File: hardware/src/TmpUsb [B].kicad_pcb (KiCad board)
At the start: 2 copper layers, 25 x 17 mm, 16 parts, among them P1 48037-2200, U1 PIC18F26J50

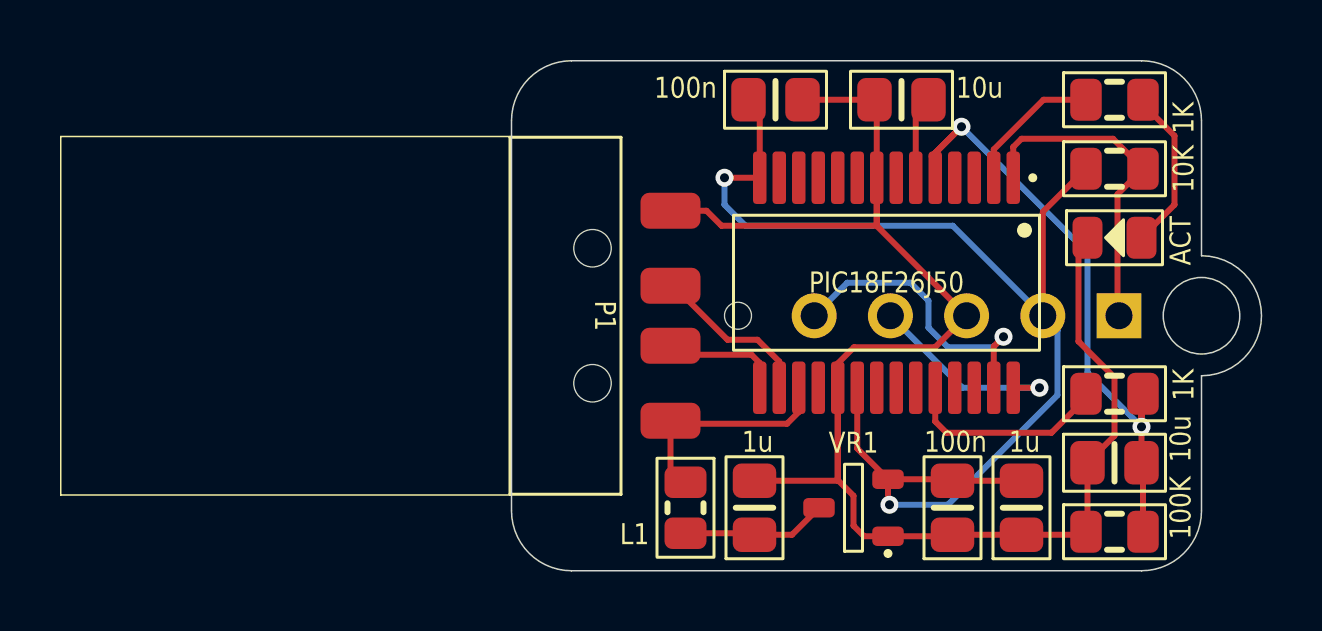
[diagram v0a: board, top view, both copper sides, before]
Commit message: Fixed USB connector DRC checks
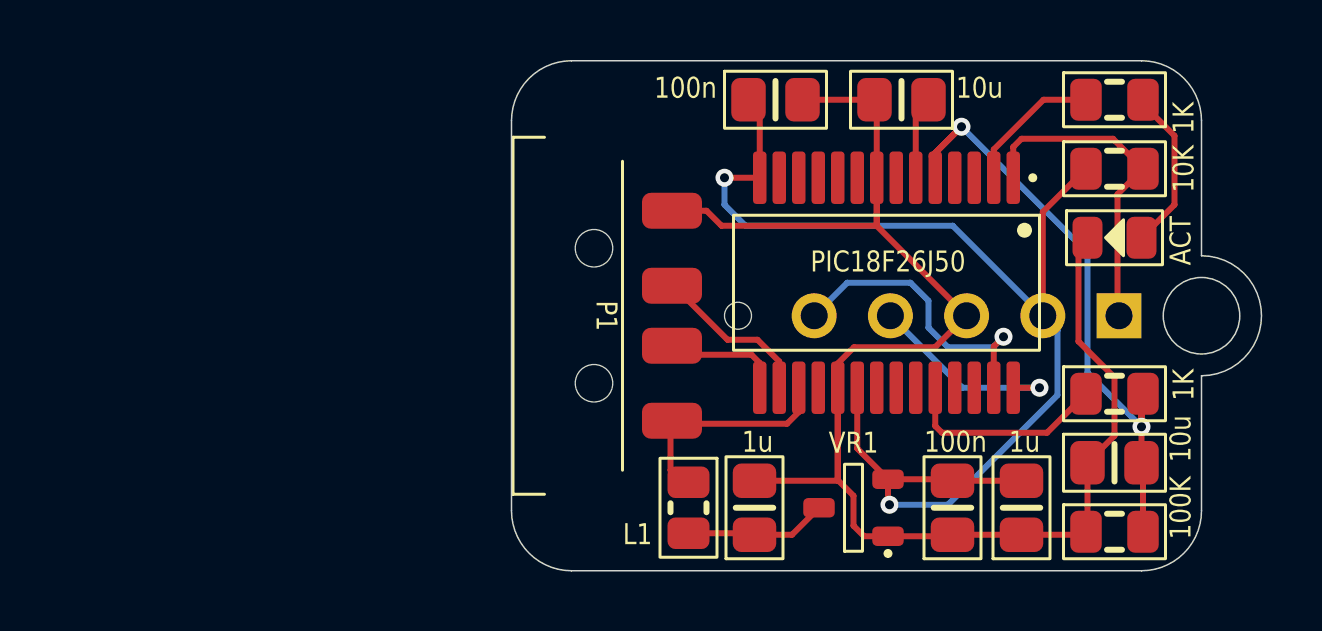
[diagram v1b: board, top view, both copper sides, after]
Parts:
- moved L1 0.10 mm to (25.9, 34.9)
- moved P1 0.05 mm to (22.8, 28.5)
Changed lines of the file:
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@@
   )
   (footprint "Medo64-SMD:L (0805)" (layer "F.Cu")
-    (at 25.8 34.9 -90)
+    (at 25.9 34.9 -90)
     (descr "RESC2013X70N")
     (attr smd)
@@
   )
   (footprint "Medo64-SMD:P USB 2.0 (4w)" (layer "F.Cu")
-    (at 22.7 28.5 -90)
+    (at 22.75 28.5 -90)
     (attr smd)
     (fp_text reference "P1" (at 0 0 -90 unlocked) (layer "F.SilkS")
@@
     (fp_text value "48037-2200" (at 0 0.825 -90 unlocked) (layer "F.SilkS") hide
         (effects (font (size 0.7 0.6) (thickness 0.1)) (justify top))
+    )
+    (fp_text user "D-" (at 1 -1.5 -90 unlocked) (layer "User.7")
+        (effects (font (size 0.13 0.07) (thickness 0.01)) (justify top))
+    )
+    (fp_text user "Vbus" (at 3.5 -1.5 -90 unlocked) (layer "User.7")
+        (effects (font (size 0.13 0.07) (thickness 0.014) bold) (justify top))
+    )
+    (fp_text user "D+" (at -1 -1.5 -90 unlocked) (layer "User.7")
+        (effects (font (size 0.13 0.07) (thickness 0.01)) (justify top))
     )
     (fp_text user "GND" (at -3.5 -1.5 -90 unlocked) (layer "User.7")
         (effects (font (size 0.13 0.07) (thickness 0.014) bold) (justify top))
     )
-    (fp_text user "D+" (at -1 -1.5 -90 unlocked) (layer "User.7")
-        (effects (font (size 0.13 0.07) (thickness 0.01)) (justify top))
-    )
-    (fp_text user "Vbus" (at 3.5 -1.5 -90 unlocked) (layer "User.7")
-        (effects (font (size 0.13 0.07) (thickness 0.014) bold) (justify top))
-    )
-    (fp_text user "D-" (at 1 -1.5 -90 unlocked) (layer "User.7")
-        (effects (font (size 0.13 0.07) (thickness 0.01)) (justify top))
-    )
-    (fp_line (start -5.975 2.75) (end -5.975 17.725)
-      (stroke (width 0.05) (type default)) (layer "F.SilkS"))
-    (fp_line (start -5.975 17.725) (end 5.975 17.725)
-      (stroke (width 0.05) (type default)) (layer "F.SilkS"))
-    (fp_line (start -5.95 -0.95) (end -5.95 2.75)
+    (fp_line (start -5.95 1.65) (end -5.95 2.7)
       (stroke (width 0.1) (type default)) (layer "F.SilkS"))
-    (fp_line (start -5.95 -0.95) (end 5.95 -0.95)
+    (fp_line (start -5.95 2.7) (end 5.95 2.7)
       (stroke (width 0.1) (type default)) (layer "F.SilkS"))
-    (fp_line (start -5.95 2.75) (end 5.95 2.75)
+    (fp_line (start -5.15 -0.95) (end 5.15 -0.95)
       (stroke (width 0.1) (type default)) (layer "F.SilkS"))
-    (fp_line (start 5.95 -0.95) (end 5.95 2.75)
+    (fp_line (start 5.95 1.65) (end 5.95 2.7)
       (stroke (width 0.1) (type default)) (layer "F.SilkS"))
-    (fp_line (start 5.975 2.75) (end 5.975 17.725)
-      (stroke (width 0.05) (type default)) (layer "F.SilkS"))
-    (fp_rect (start -7 -4.1) (end 7 18.25)
-      (stroke (width 0.01) (type dash)) (fill none) (layer "F.CrtYd"))
+    (fp_line (start -7 -2.1) (end -4.6 -2.1)
+      (stroke (width 0.01) (type dash)) (layer "F.CrtYd"))
+    (fp_line (start -7 18.25) (end -7 -2.1)
+      (stroke (width 0.01) (type dash)) (layer "F.CrtYd"))
+    (fp_line (start -7 18.25) (end 7 18.25)
+      (stroke (width 0.01) (type dash)) (layer "F.CrtYd"))
+    (fp_line (start -4.6 -4.1) (end 4.6 -4.1)
+      (stroke (width 0.01) (type dash)) (layer "F.CrtYd"))
+    (fp_line (start -4.6 -2.1) (end -4.6 -4.1)
+      (stroke (width 0.01) (type dash)) (layer "F.CrtYd"))
+    (fp_line (start 4.6 -2.1) (end 4.6 -4.1)
+      (stroke (width 0.01) (type dash)) (layer "F.CrtYd"))
+    (fp_line (start 4.6 -2.1) (end 7 -2.1)
+      (stroke (width 0.01) (type dash)) (layer "F.CrtYd"))
+    (fp_line (start 7 18.25) (end 7 -2.1)
+      (stroke (width 0.01) (type dash)) (layer "F.CrtYd"))
+    (fp_line (start -6 2.75) (end 6 2.75)
+      (stroke (width 0.01) (type dash_dot)) (layer "F.Fab"))
     (fp_rect (start -6 17.75) (end 6 -1)
       (stroke (width 0.01) (type dash_dot)) (fill none) (layer "F.Fab"))
@@
     (pad "4" smd roundrect (at -3.5 -2.6 270) (size 1.2 2) (layers "F.Cu" "F.Paste" "F.Mask") (roundrect_rratio 0.25)
       (net 5 "GND") (thermal_bridge_angle 45))
-    (model "Models/480372200.stp"
+    (model "../../3dmodels/Medo64-SMD.3dshapes/480372200.step"
       (offset (xyz 0 -8.375 0))
       (scale (xyz 1 1 1))
@@
         (effects (font (size 0.7 0.6) (thickness 0.1)) (justify bottom))
     )
-    (fp_text value "PIC18F26J50" (at 0 0 unlocked) (layer "F.SilkS")
+    (fp_text value "PIC18F26J50" (at -0.7 -0.05 unlocked) (layer "F.SilkS")
         (effects (font (size 0.7 0.6) (thickness 0.1)))
     )
@@
   (segment (start 39.2 26.4) (end 39.2 30.4) (width 0.2) (layer "B.Cu") (net 7))
   (segment (start 35 22.2) (end 39.2 26.4) (width 0.2) (layer "B.Cu") (net 7))
-  (segment (start 39.15 31.25) (end 38 32.4) (width 0.2) (layer "F.Cu") (net 8))
-  (segment (start 34.5 32.4) (end 34.125 32.025) (width 0.2) (layer "F.Cu") (net 8))
-  (segment (start 34.125 31.125) (end 34.2 31.2) (width 0.2) (layer "F.Cu") (net 8))
-  (segment (start 39.15 31.1) (end 39.15 31.25) (width 0.2) (layer "F.Cu") (net 8))
-  (segment (start 38 32.4) (end 34.5 32.4) (width 0.2) (layer "F.Cu") (net 8))
-  (segment (start 34.125 32.025) (end 34.125 30.9) (width 0.2) (layer "F.Cu") (net 8))
-  (segment (start 34.125 30.9) (end 34.125 31.125) (width 0.2) (layer "F.Cu") (net 8))
+  (segment (start 34.125 32.175) (end 34.35 32.4) (width 0.2) (layer "F.Cu") (net 8))
+  (segment (start 34.125 30.9) (end 34.125 32.175) (width 0.2) (layer "F.Cu") (net 8))
+  (segment (start 34.35 32.4) (end 37.85 32.4) (width 0.2) (layer "F.Cu") (net 8))
+  (segment (start 37.85 32.4) (end 39.15 31.1) (width 0.2) (layer "F.Cu") (net 8))
   (segment (start 41.05 23.6) (end 40.2 24.45) (width 0.2) (layer "F.Cu") (net 9))
   (segment (start 40.05 22.6) (end 37 22.6) (width 0.2) (layer "F.Cu") (net 9))

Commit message: Cleaning up traces and adding copper pour
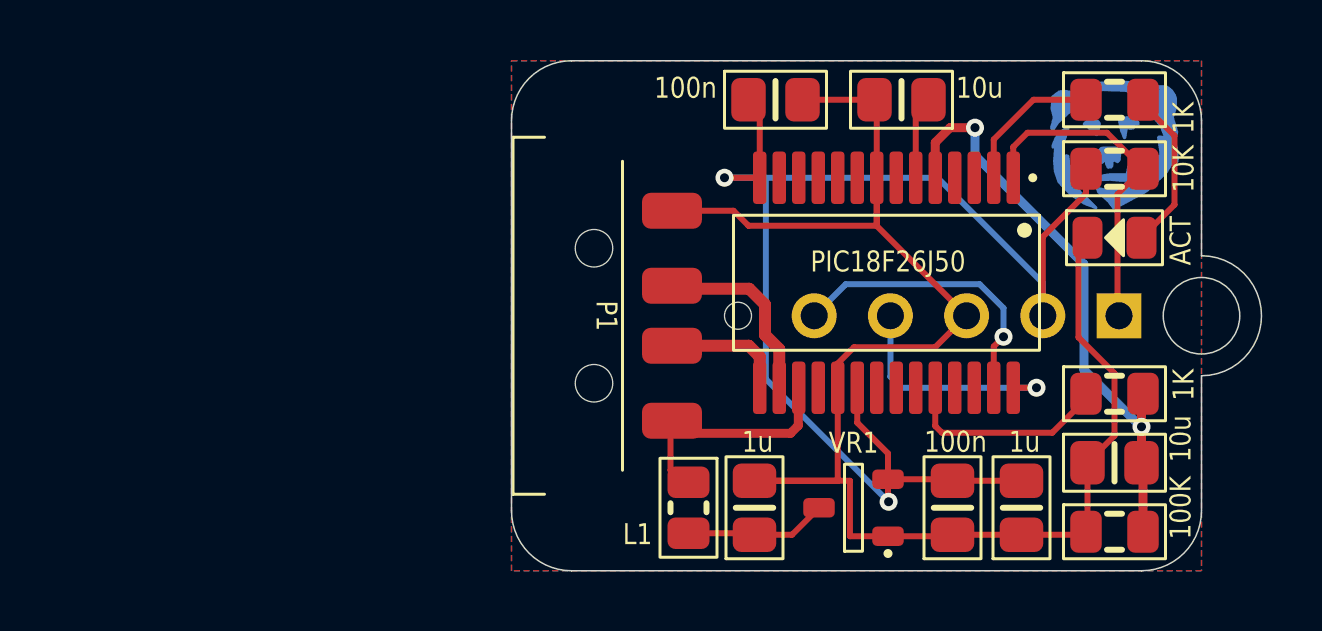
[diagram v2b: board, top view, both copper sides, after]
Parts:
- added Z?: Medo64, Medo64-SMD:Z Icon [Medo64], B.Cu at (40.1, 22.8)
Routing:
- net 3V3: track 40.8 -> 44.2 mm
- net GND: track 55.2 -> 53.8 mm
- net CAP: track 21.7 -> 20.5 mm
- net PGD: track 6.84 -> 7.83 mm
- net USB_D+: track 5.15 -> 5.84 mm
- net VCAP: track 2.38 -> 1.77 mm
- added copper zone on B.Cu, net GND
- added copper zone on F.Cu, net GND
